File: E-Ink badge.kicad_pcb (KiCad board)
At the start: 2 copper layers, 41 x 32.5 mm, 7 parts, among them J2 E-INK-FPC, Q1 BSS138, U1 RP2040, U2 AP2112K-3.3

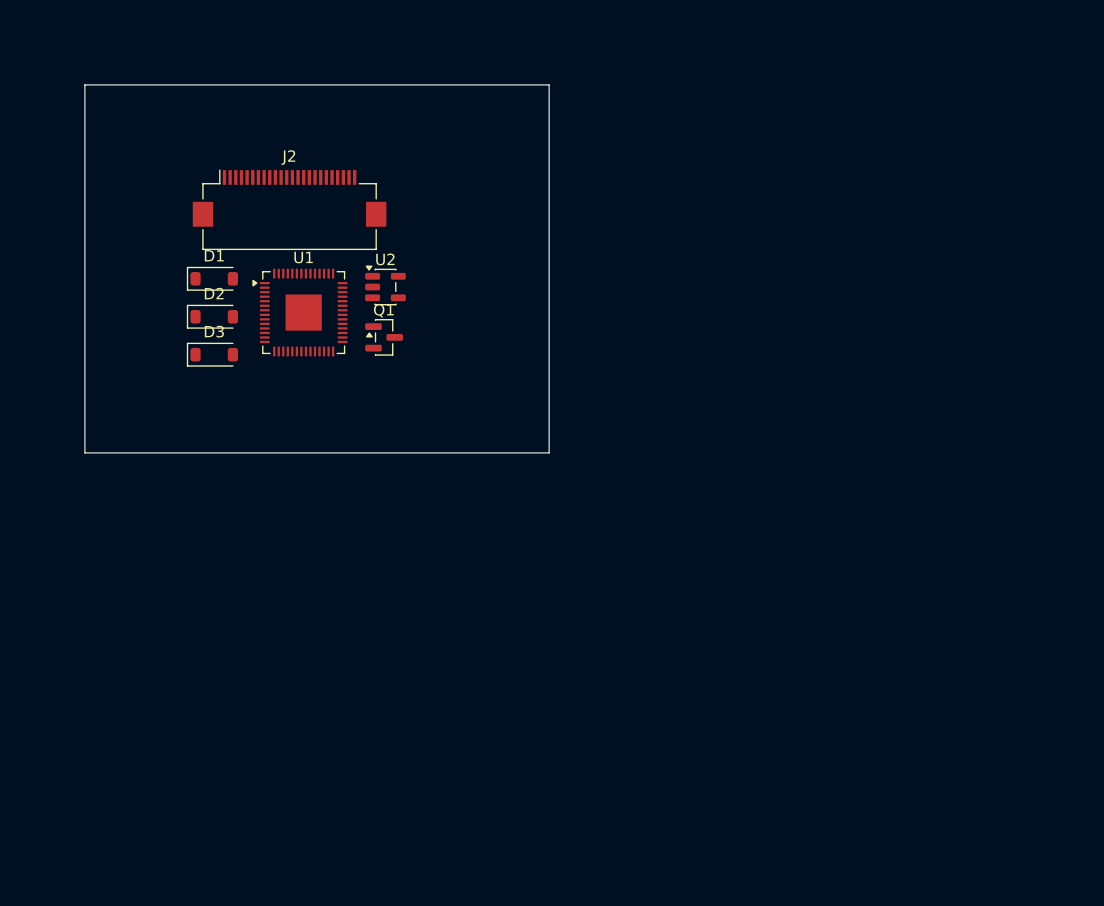
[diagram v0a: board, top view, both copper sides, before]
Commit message: Continued routing the PCB
routed parts of the MCU, most of the FPC Cable and stuff like that.
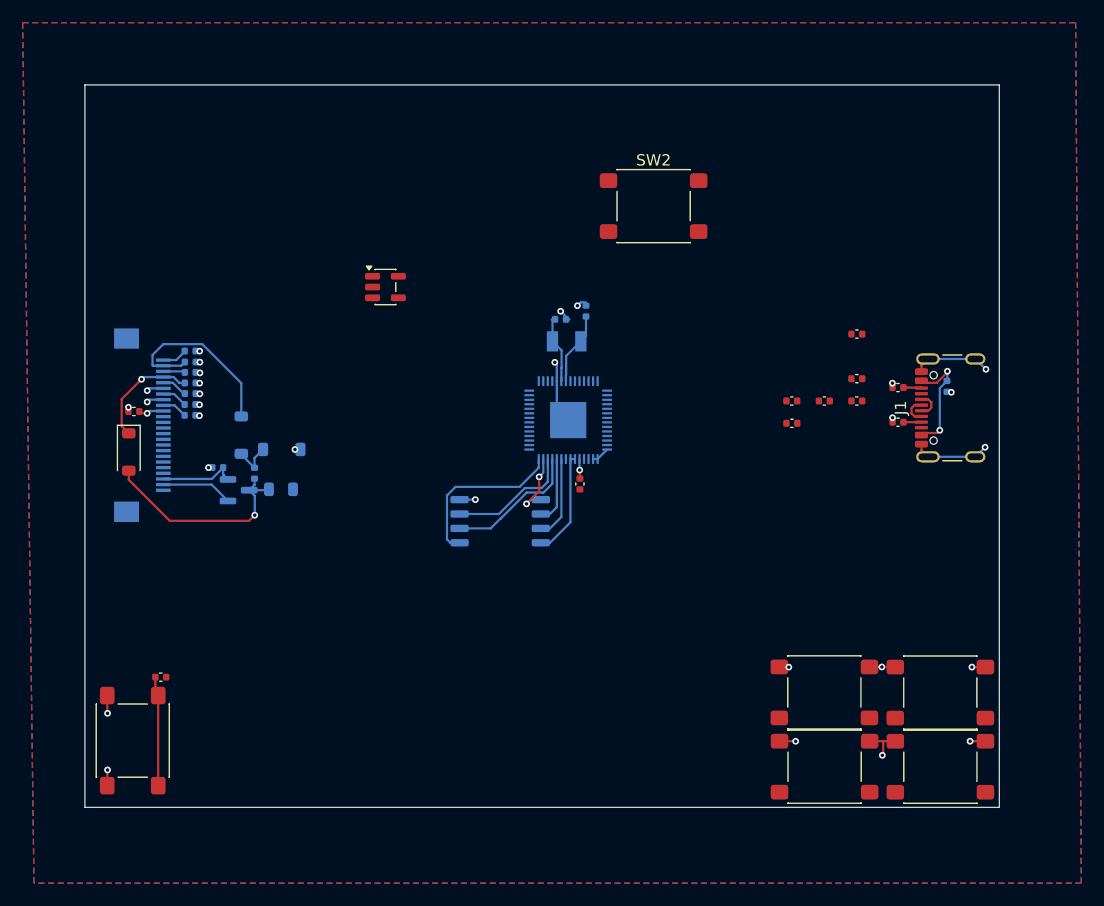
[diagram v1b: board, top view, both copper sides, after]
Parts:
- added C1: 0.1uF, Capacitor_SMD:C_0402_1005Metric, B.Cu at (194.6, 96.1)
- added C10: 4.7µF, Capacitor_SMD:C_0402_1005Metric, B.Cu at (127.8, 93.0)
- added C11: 4.7µF, Capacitor_SMD:C_0402_1005Metric, B.Cu at (127.8, 94.0)
- added C12: 4.7µF, Capacitor_SMD:C_0402_1005Metric, B.Cu at (127.8, 94.9)
- added C13: 12pF, Capacitor_SMD:C_0402_1005Metric, B.Cu at (160.5, 90.2)
- added C14: 12pF, Capacitor_SMD:C_0402_1005Metric, B.Cu at (162.8, 89.5)
- added C15: 0.1µF, Capacitor_SMD:C_0402_1005Metric, F.Cu at (183.8, 97.4)
- added C2: 0.1uF, Capacitor_SMD:C_0402_1005Metric, F.Cu at (122.8, 98.3)
- added C3: 1uF, Capacitor_SMD:C_0402_1005Metric, B.Cu at (127.8, 98.7)
- added C4: 1uF, Capacitor_SMD:C_0402_1005Metric, B.Cu at (127.8, 97.7)
- added C5: 4.7µF, Capacitor_SMD:C_0402_1005Metric, B.Cu at (133.5, 103.8)
- added C6: 4.7µF, Capacitor_SMD:C_0402_1005Metric, F.Cu at (180.9, 97.4)
- added C7: 4.7µF, Capacitor_SMD:C_0402_1005Metric, F.Cu at (180.9, 99.4)
- added C8: 4.7µF, Capacitor_SMD:C_0402_1005Metric, B.Cu at (127.8, 96.8)
- added C9: 4.7µF, Capacitor_SMD:C_0402_1005Metric, B.Cu at (127.8, 95.8)
- added J1: USB_C_Receptacle_USB2.0_14P, Connector_USB:USB_C_Receptacle_GCT_USB4105-xx-A_16P_TopMnt_Horizontal, F.Cu at (196.1, 98.0)
- added L1: 10µH, Inductor_SMD:L_0805_2012Metric, B.Cu at (135.8, 105.2)
- added R1: 0.47Ω, Capacitor_SMD:C_0402_1005Metric, B.Cu at (130.2, 103.3)
- added R2: 5.1kΩ, Capacitor_SMD:C_0402_1005Metric, F.Cu at (190.3, 99.3)
- added R3: 5.1kΩ, Capacitor_SMD:C_0402_1005Metric, F.Cu at (190.3, 96.2)
- added R4: 10kΩ, Capacitor_SMD:C_0402_1005Metric, F.Cu at (186.7, 91.5)
- added R5: 1kΩ, Capacitor_SMD:C_0402_1005Metric, F.Cu at (125.2, 121.8)
- added R6: 10kΩ, Capacitor_SMD:C_0402_1005Metric, F.Cu at (186.7, 95.4)
- added R7: 27Ω, Capacitor_SMD:C_0402_1005Metric, F.Cu at (186.7, 97.4)
- added R8: 27Ω, Capacitor_SMD:C_0402_1005Metric, F.Cu at (162.2, 104.7)
- added SW1: BOOTSEL, Button_Switch_SMD:SW_SPST_PTS645Sx43SMTR92, F.Cu at (122.7, 127.4)
- added SW2: RUN, Button_Switch_SMD:SW_SPST_PTS645Sx43SMTR92, F.Cu at (168.7, 80.2)
- added SW3: W, Button_Switch_SMD:SW_SPST_PTS645Sx43SMTR92, F.Cu at (194.0, 123.2)
- added SW4: A, Button_Switch_SMD:SW_SPST_PTS645Sx43SMTR92, F.Cu at (183.8, 123.2)
- added SW5: S, Button_Switch_SMD:SW_SPST_PTS645Sx43SMTR92, F.Cu at (183.8, 129.7)
- added SW6: D, Button_Switch_SMD:SW_SPST_PTS645Sx43SMTR92, F.Cu at (194.1, 129.7)
- added U3: W25Q16JVSS, Package_SO:SOIC-8_5.3x5.3mm_P1.27mm, B.Cu at (155.2, 108.0)
- added Y1: Crystal, Crystal:Crystal_SMD_3215-2Pin_3.2x1.5mm, B.Cu at (161.0, 92.1)
- D2, D3, J2, Q1, U1: moved to B.Cu
- moved U1 25.2 mm to (161.2, 99.1)
- moved J2 23.9 mm to (123.6, 99.5), turned to 90 degrees
- moved Q1 18.6 mm to (132.1, 105.3)
- moved D1 17.1 mm to (122.4, 101.9), turned to -90 degrees
- moved D2 13.1 mm to (135.9, 101.7), turned to 180 degrees
- moved D3 7.49 mm to (132.3, 100.4), turned to 90 degrees
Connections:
- D2 pad 1: unconnected-(D2-K-Pad1) -> GND
- D2 pad 2: unconnected-(D2-A-Pad2) -> Net-(D2-A)
- D3 pad 1: unconnected-(D3-K-Pad1) -> Net-(D2-A)
- D3 pad 2: unconnected-(D3-A-Pad2) -> PREVGL
- U1 pad 1: Net-(U1-IOVDD-Pad1) -> +3.3V
- U1 pad 10: Net-(U1-IOVDD-Pad1) -> +3.3V
- U1 pad 19: unconnected-(U1-TESTEN-Pad19) -> GND
- U1 pad 2: unconnected-(U1-GPIO0-Pad2) -> GPIO_W
- U1 pad 22: Net-(U1-IOVDD-Pad1) -> +3.3V
- U1 pad 23: Net-(U1-DVDD-Pad23) -> Net-(U1-VREG_VOUT)
- U1 pad 26: unconnected-(U1-RUN-Pad26) -> RUN
- U1 pad 3: unconnected-(U1-GPIO1-Pad3) -> GPIO_A
- U1 pad 33: Net-(U1-IOVDD-Pad1) -> +3.3V
- U1 pad 4: unconnected-(U1-GPIO2-Pad4) -> GPIO_S
- U1 pad 42: Net-(U1-IOVDD-Pad1) -> +3.3V
- U1 pad 43: unconnected-(U1-ADC_AVDD-Pad43) -> +3.3V
- U1 pad 44: unconnected-(U1-VREG_VIN-Pad44) -> +3.3V
- U1 pad 45: unconnected-(U1-VREG_VOUT-Pad45) -> Net-(U1-VREG_VOUT)
- U1 pad 46: D- -> Net-(U1-USB_DM)
- U1 pad 47: D+ -> Net-(U1-USB_DP)
- U1 pad 48: unconnected-(U1-USB_VDD-Pad48) -> +3.3V
- U1 pad 49: Net-(U1-IOVDD-Pad1) -> +3.3V
- U1 pad 5: unconnected-(U1-GPIO3-Pad5) -> GPIO_D
- U1 pad 50: Net-(U1-DVDD-Pad23) -> Net-(U1-VREG_VOUT)
- U1 pad 51: unconnected-(U1-QSPI_SD3-Pad51) -> QSPI_SD3
- U1 pad 52: unconnected-(U1-QSPI_SCLK-Pad52) -> QSPI_SCLK
- U1 pad 53: unconnected-(U1-QSPI_SD0-Pad53) -> QSPI_SD0
- U1 pad 54: unconnected-(U1-QSPI_SD2-Pad54) -> QSPI_SD2
- U1 pad 55: unconnected-(U1-QSPI_SD1-Pad55) -> QSPI_SD1
- U1 pad 56: unconnected-(U1-~{QSPI_SS}-Pad56) -> BOOTSEL
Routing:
- net GND: track 0.00 -> 44.2 mm, vias 0 -> 29
- net Net-(D1-A): track 0.00 -> 19.0 mm, vias 0 -> 1
- net PREVGL: track 0.00 -> 16.5 mm
- net +3.3V: track 0.00 -> 15.5 mm, vias 0 -> 1
- net BOOTSEL: track 0.00 -> 15.0 mm
- net QSPI_SD0: track 0.00 -> 12.0 mm
- net QSPI_SD2: track 0.00 -> 11.0 mm
- net Net-(U2-EN): track 0.00 -> 10.1 mm, vias 0 -> 2
- net PREVGH: track 0.00 -> 9.88 mm, vias 0 -> 1
- net Net-(R5-Pad1): track 0.00 -> 9.69 mm
- net QSPI_SD3: track 0.00 -> 7.35 mm
- net RESE: track 0.00 -> 6.93 mm
- net GDR: track 0.00 -> 6.31 mm
- net Net-(U1-XOUT): track 0.00 -> 6.15 mm
- net QSPI_SD1: track 0.00 -> 5.99 mm, vias 0 -> 2
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- added copper zone on B.Cu, net GND
- added copper zone on F.Cu, net GND
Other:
- board size 41 x 32.5 mm -> 80.8 x 63.8 mm

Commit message: Finally finished routing the whole board!
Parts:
- C15, C6, C7, R4: moved to B.Cu
- moved R6 64.3 mm to (133.5, 131.5), turned to 90 degrees
- moved SW2 61.3 mm to (129.6, 127.4), turned to 90 degrees
- moved C1 57.2 mm to (137.7, 90.9), turned to 180 degrees
- moved J1 57.1 mm to (139.6, 89.4), turned to 180 degrees
- moved C6 55.5 mm to (127.5, 112.7), turned to 180 degrees
- moved C7 55.3 mm to (127.5, 113.6), turned to 180 degrees
- moved R3 52.5 mm to (137.8, 95.2), turned to -90 degrees
- moved R2 49.6 mm to (140.9, 95.2), turned to -90 degrees
- moved R7 46.9 mm to (139.9, 95.2), turned to -90 degrees
- moved C15 37.1 mm to (146.7, 99.4), turned to 180 degrees
- moved C14 35.4 mm to (144.7, 119.9), turned to -90 degrees
- moved C13 32.0 mm to (147.0, 119.2), turned to 180 degrees
- moved R4 29.8 mm to (157.9, 99.4), turned to 180 degrees
- moved Y1 29.0 mm to (146.5, 117.2), turned to 0 degrees
- moved R8 25.3 mm to (138.8, 95.2), turned to 90 degrees
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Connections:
- U1 pad 11: unconnected-(U1-GPIO8-Pad11) -> GPIO_W
- U1 pad 12: unconnected-(U1-GPIO9-Pad12) -> GPIO_A
- U1 pad 13: unconnected-(U1-GPIO10-Pad13) -> GPIO_D
- U1 pad 14: unconnected-(U1-GPIO11-Pad14) -> GPIO_S
- U1 pad 2: GPIO_W -> unconnected-(U1-GPIO0-Pad2)
- U1 pad 3: GPIO_A -> unconnected-(U1-GPIO1-Pad3)
- U1 pad 4: GPIO_S -> unconnected-(U1-GPIO2-Pad4)
- U1 pad 5: GPIO_D -> unconnected-(U1-GPIO3-Pad5)
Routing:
- net BOOTSEL: track 15.0 -> 66.4 mm, vias 0 -> 1
- net GPIO_D: track 0.00 -> 40.5 mm, vias 0 -> 1
- net GPIO_W: track 0.00 -> 34.4 mm, vias 0 -> 1
- net GPIO_S: track 0.00 -> 31.1 mm, vias 0 -> 1
- net GPIO_A: track 0.00 -> 27.9 mm, vias 0 -> 1
- net RUN: track 0.00 -> 27.3 mm, vias 0 -> 1
- net CS: track 0.00 -> 24.0 mm, vias 0 -> 2
- net MOSI: track 0.00 -> 23.1 mm, vias 0 -> 2
- net DC: track 0.00 -> 22.0 mm, vias 0 -> 2
- net CLK: track 0.00 -> 20.6 mm, vias 0 -> 2
- net RST: track 0.00 -> 18.8 mm, vias 0 -> 2
- net BUSY: track 0.00 -> 17.7 mm
- net Net-(U1-USB_DM): track 0.00 -> 13.9 mm, vias 0 -> 1
- net Net-(U1-USB_DP): track 1.74 -> 14.0 mm
- net Net-(U1-VREG_VOUT): track 0.00 -> 11.5 mm
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- added copper zone on F.Cu, net +3.3V
- removed copper zone on F.Cu, net GND
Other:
- board size 80.8 x 63.8 mm -> 61.7 x 46.8 mm
- board text added: "W A S D"

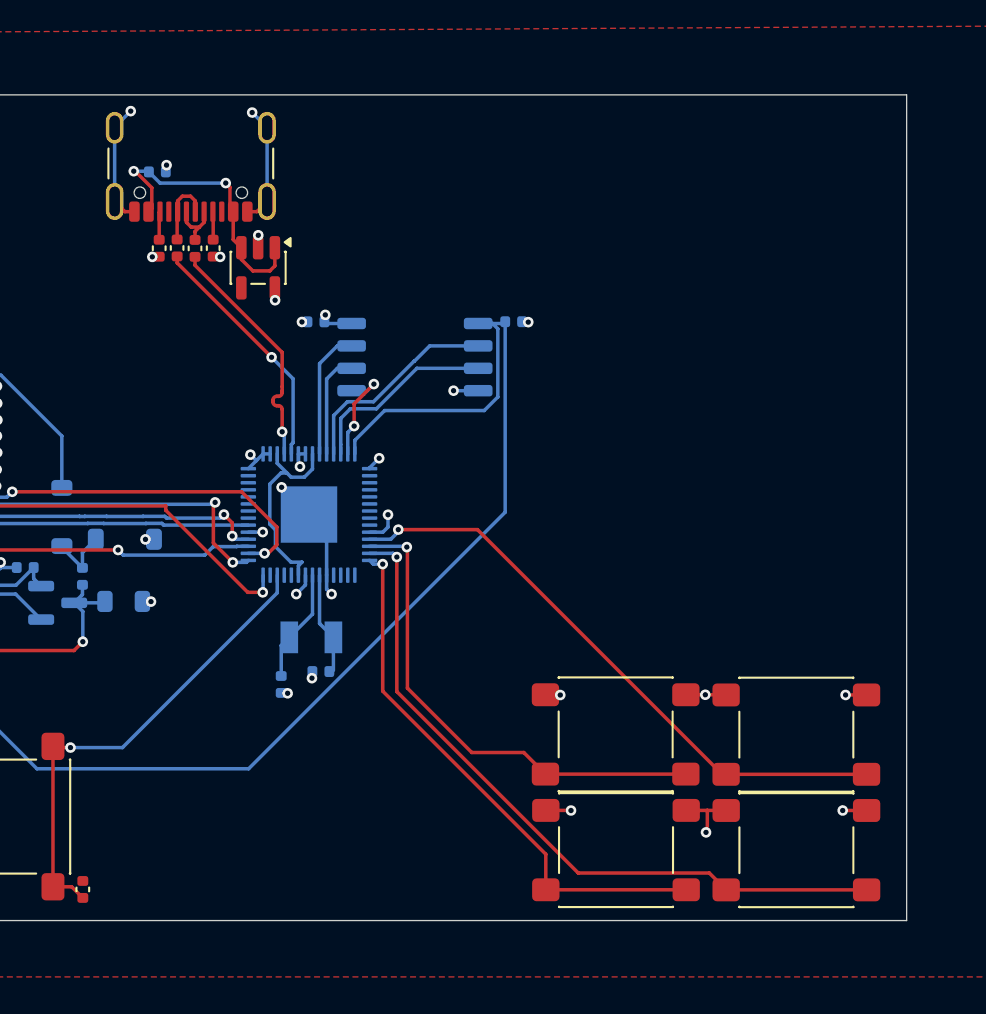
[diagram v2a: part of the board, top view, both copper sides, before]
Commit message: Finished some PCB art + updated prod files
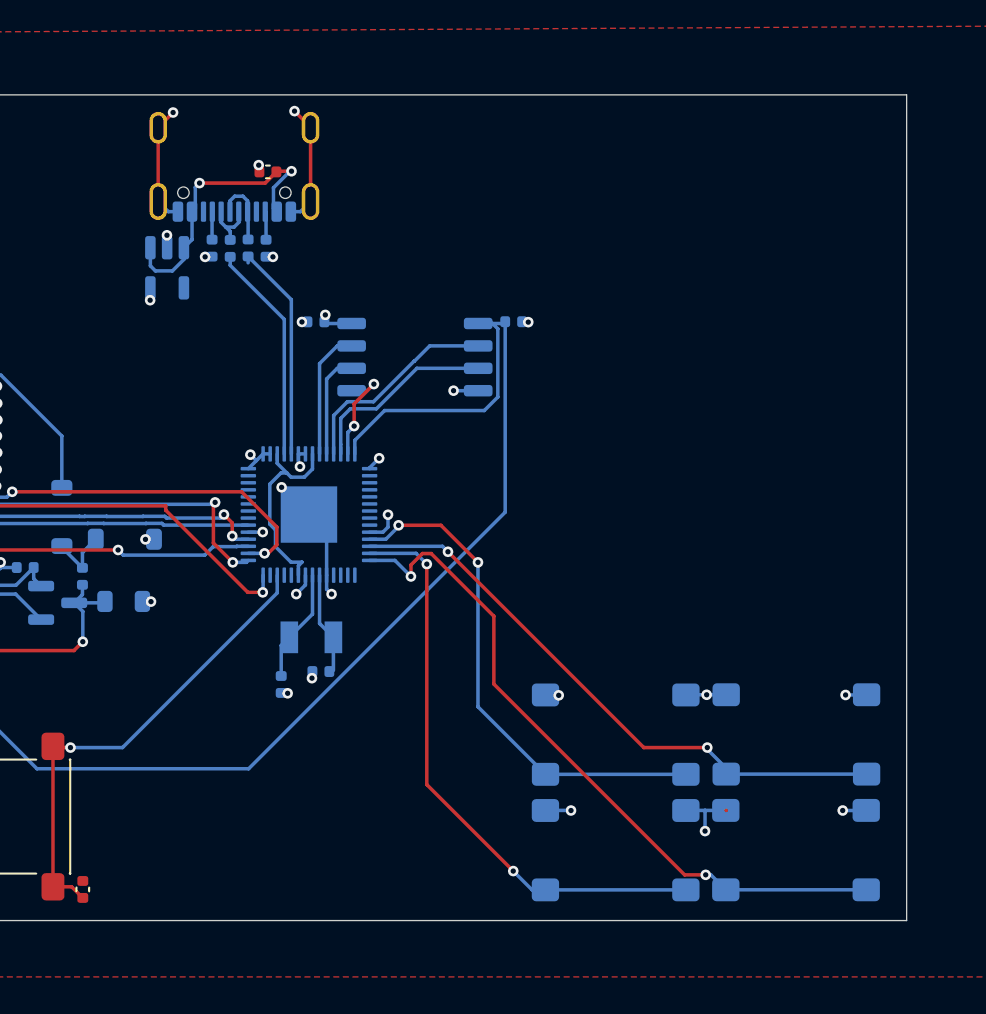
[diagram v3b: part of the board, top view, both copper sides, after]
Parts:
- C1: moved to F.Cu
- J1, R2, R3, R7, R8, SW3, SW4, SW5, SW6, U2: moved to B.Cu
- moved SW6 10.2 mm to (163.7, 129.3), turned to 180 degrees
- moved SW4 10.2 mm to (174.0, 122.8), turned to 180 degrees
- moved SW3 10.2 mm to (163.7, 122.8), turned to 180 degrees
- moved SW5 10.2 mm to (173.9, 129.3), turned to 180 degrees
- moved C1 6.27 mm to (144.0, 90.9), turned to 0 degrees
- moved R3 6.06 mm to (143.9, 95.2)
- moved U2 5.16 mm to (138.3, 96.3)
- moved R8 4.02 mm to (142.9, 95.2)
- moved J1 2.47 mm to (142.1, 89.4), turned to 0 degrees
- moved R7 1.99 mm to (141.9, 95.2)
- moved R2 0.06 mm to (140.8, 95.2)
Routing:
- net GPIO_S: track 31.1 -> 39.6 mm, vias 1 -> 2
- net GPIO_D: track 40.5 -> 33.2 mm, vias 1 -> 2
- net GPIO_A: track 27.9 -> 33.8 mm, vias 1 -> 2
- net GPIO_W: track 34.4 -> 28.9 mm, vias 1 -> 2
- net Net-(U1-USB_DM): track 13.9 -> 12.4 mm, vias 1 -> 0
- net Net-(U1-USB_DP): track 14.0 -> 12.6 mm, vias 1 -> 0
- net GND: track 48.9 -> 48.0 mm
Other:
- board text removed: "W A S D"
